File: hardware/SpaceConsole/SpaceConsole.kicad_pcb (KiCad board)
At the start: 2 copper layers, 10 parts, among them IC1 ArduinoProMini, J1 Screw_Terminal_01x03, J2 Screw_Terminal_01x03, J3 Screw_Terminal_01x03, J4 Screw_Terminal_01x03, J5 Screw_Terminal_01x03, J6 Screw_Terminal_01x02, J7 Screw_Terminal_01x02, J8 Conn_01x09_Male, U1 LM2596_Adj_Stepdown_Module

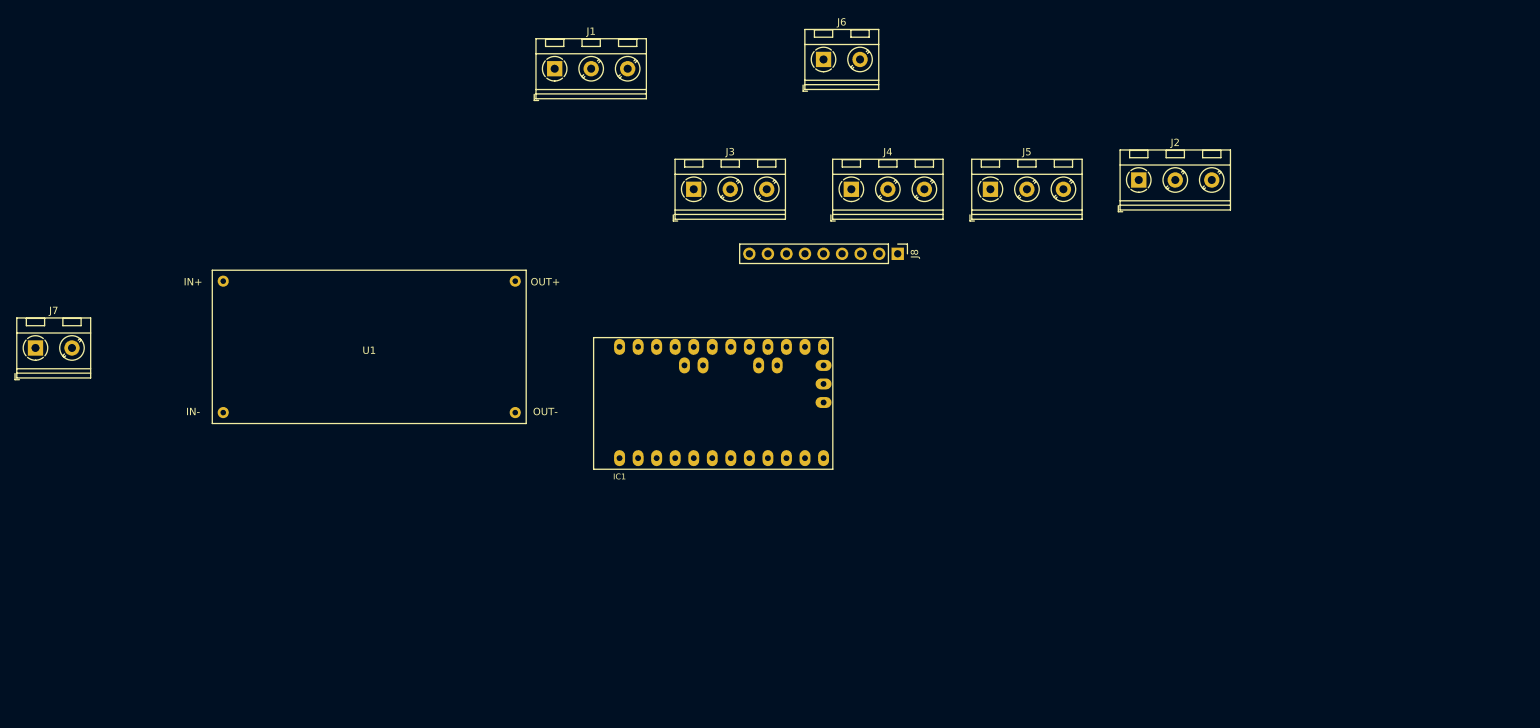
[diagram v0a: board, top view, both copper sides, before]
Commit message: PCB layed out (no traces yet)
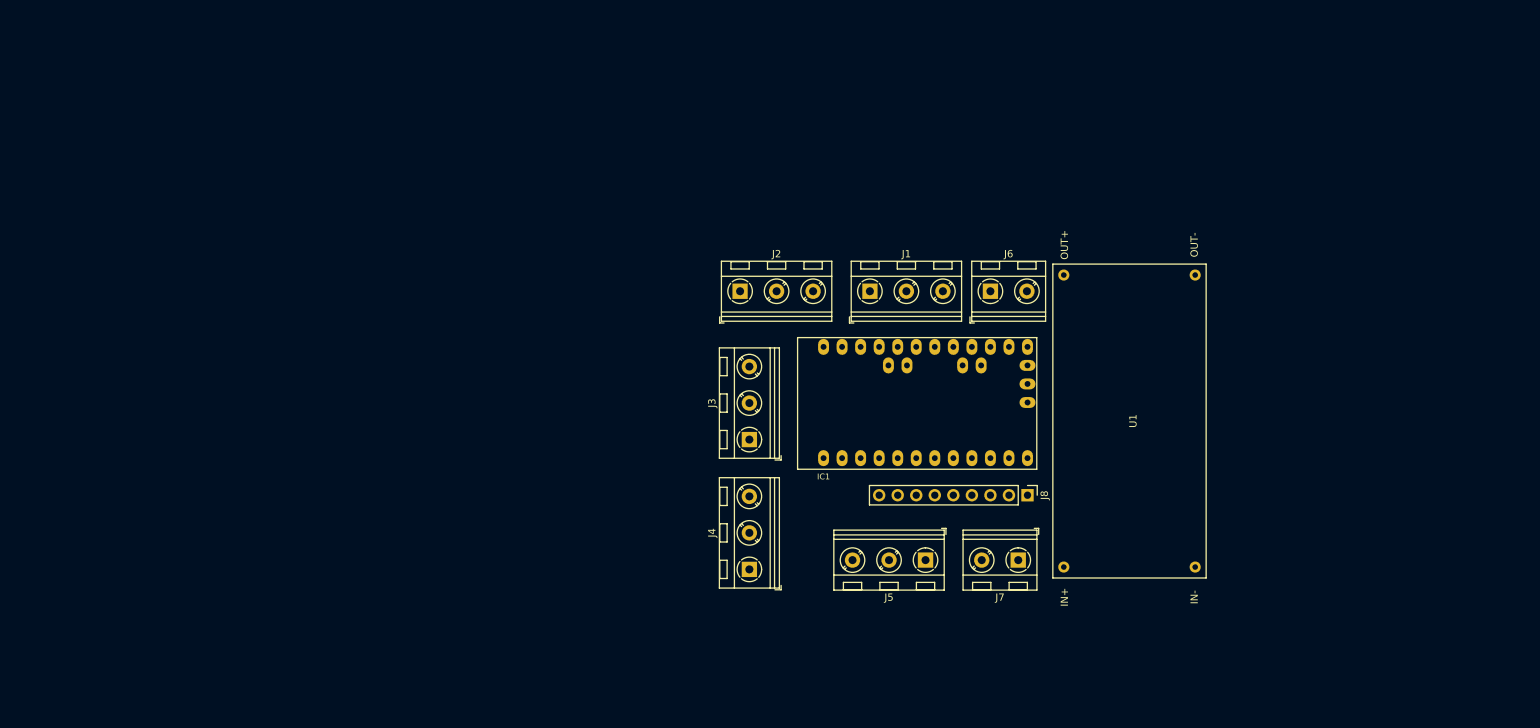
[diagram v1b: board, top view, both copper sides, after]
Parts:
- J1: value Screw_Terminal_01x03 -> LeftFrontLED
- J2: value Screw_Terminal_01x03 -> RightFrontLED
- J3: value Screw_Terminal_01x03 -> LeftMiddleLED
- J4: value Screw_Terminal_01x03 -> RightMiddleLED
- J5: value Screw_Terminal_01x03 -> RearLED
- J6: value Screw_Terminal_01x02 -> SwitchA
- J7: value Screw_Terminal_01x02 -> BatteryIN
- moved J7 137.7 mm to (176.5, 120.7), turned to 180 degrees
- moved U1 104.6 mm to (191.8, 101.6), turned to 90 degrees
- moved J2 56.7 mm to (138.4, 83.8)
- moved J4 53.9 mm to (139.7, 121.9), turned to 90 degrees
- moved J1 52.9 mm to (156.2, 83.8)
- moved J5 51.6 mm to (163.8, 120.7), turned to 180 degrees
- moved J6 39.1 mm to (172.7, 83.8)
- moved J8 37.5 mm to (177.8, 111.8)
- moved J3 35.1 mm to (139.7, 104.1), turned to 90 degrees
- moved IC1 27.9 mm to (163.8, 99.1)

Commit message: Routing done
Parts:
- moved J8 36.8 mm to (141.0, 111.8), turned to 90 degrees
- moved J6 33.0 mm to (139.7, 83.8)
- moved J2 12.7 mm to (151.1, 83.8)
- moved J1 11.4 mm to (167.6, 83.8)
- moved J4 6.48 mm to (146.1, 120.7), turned to 180 degrees
- turned IC1 to 180 degrees
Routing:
- net VCC: track 0.00 -> 109.3 mm
- net /RightMiddleLED: track 0.00 -> 52.8 mm
- net /RearLED: track 0.00 -> 30.7 mm
- net /Battery-: track 0.00 -> 30.5 mm
- net /LeftMiddleLED: track 0.00 -> 27.9 mm
- net /SwitchB: track 0.00 -> 26.7 mm
- net /SwitchC: track 0.00 -> 21.0 mm
- net /SwitchA: track 0.00 -> 18.4 mm
- net /RightFrontLED: track 0.00 -> 12.1 mm
- net /LeftFrontLED: track 0.00 -> 9.69 mm
- net /Battery+: track 0.00 -> 6.63 mm
- net /KnobB1: track 0.00 -> 5.61 mm
- net /KnobB0: track 0.00 -> 5.61 mm
- net /KnobA1: track 0.00 -> 5.61 mm
- net /KnobA0: track 0.00 -> 5.61 mm
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- added copper zone on B.Cu, net GND

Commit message: Remove extra pins from pro
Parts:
- J7: value BatteryIN -> Battery
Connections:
- IC1 pad 21: VCC -> Net-(IC1-Pad21)
- IC1 pad 23: Net-(IC1-Pad23) -> GND
- IC1 pad 24: GND -> VCC
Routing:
- net VCC: track 109.3 -> 129.0 mm

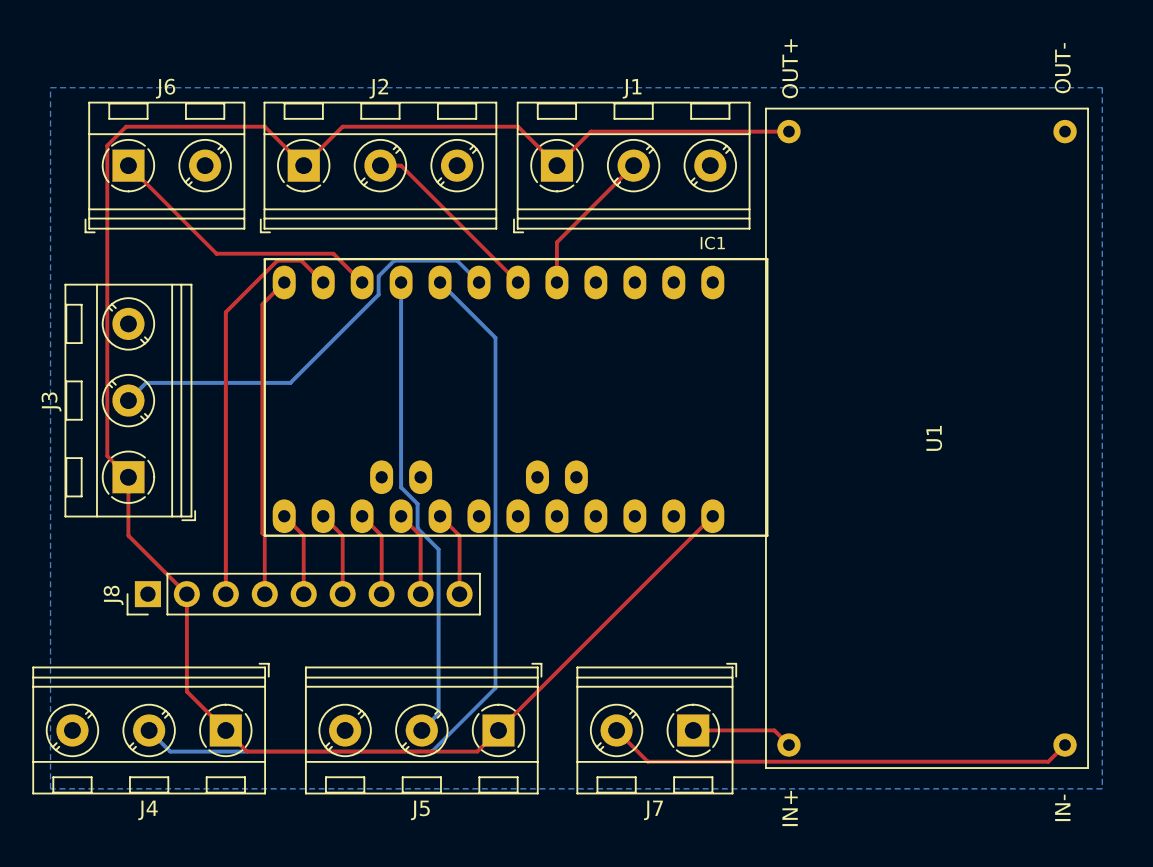
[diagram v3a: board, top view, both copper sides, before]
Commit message: Thicker power traces, add edge cutout
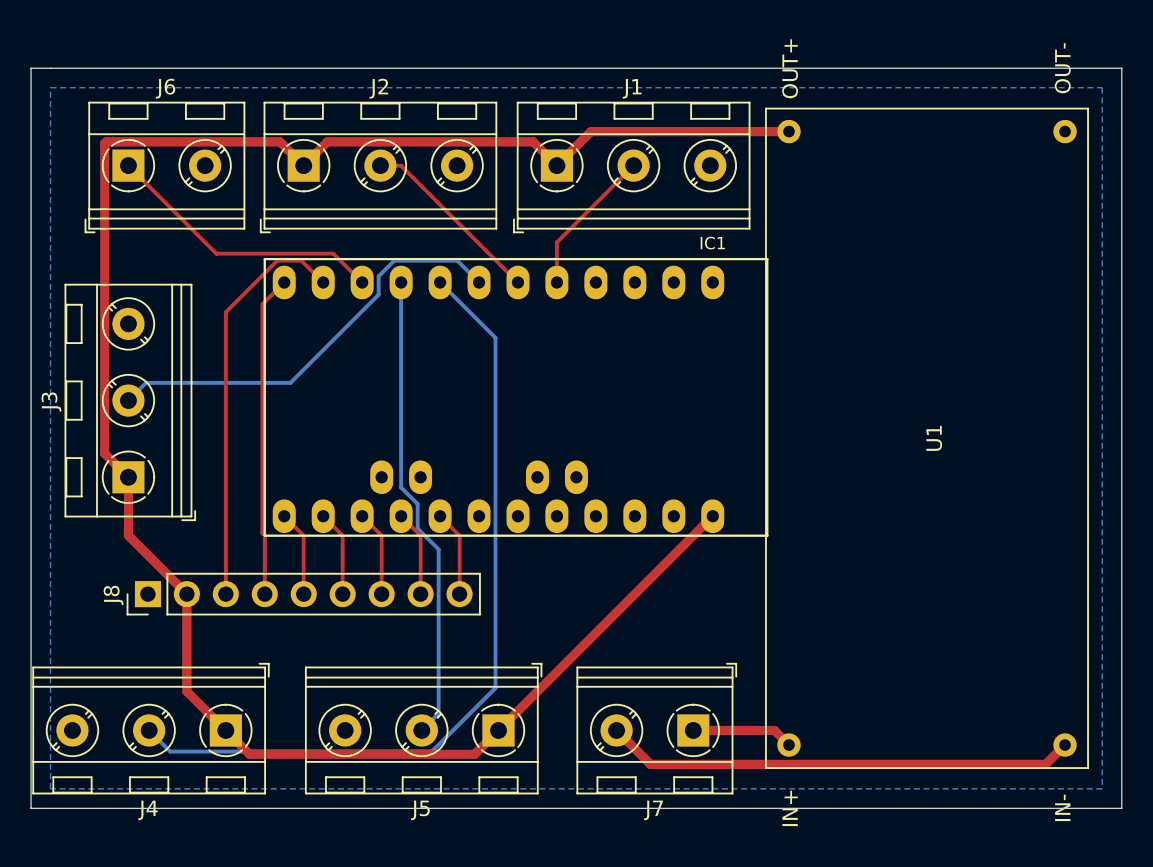
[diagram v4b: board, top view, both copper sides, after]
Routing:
- net VCC: track 129.0 -> 127.9 mm
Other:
- board outline added: 71.1 x 48.3 mm
- net class Power added: clearance 0.2, trace_width 0.6, via_dia 0.8, via_drill 0.4
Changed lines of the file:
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@@
   (general
     (thickness 1.6)
-    (drawings 0)
+    (drawings 5)
     (tracks 66)
     (zones 0)
@@
     (uvia_dia 0.3)
     (uvia_drill 0.1)
-    (add_net /Battery+)
-    (add_net /Battery-)
     (add_net /HornOut)
     (add_net /KnobA0)
@@
     (add_net "Net-(IC1-Pad3)")
     (add_net "Net-(IC1-Pad4)")
+  )
+  (net_class Power ""
+    (clearance 0.2)
+    (trace_width 0.6)
+    (via_dia 0.8)
+    (via_drill 0.4)
+    (uvia_dia 0.3)
+    (uvia_drill 0.1)
+    (add_net /Battery+)
+    (add_net /Battery-)
     (add_net VCC)
   )
@@
     )
   )
-  (segment (start 169.86 81.6) (end 167.64 83.82) (width 0.25) (layer F.Cu) (net 7))
-  (segment (start 182.77 81.6) (end 169.86 81.6) (width 0.25) (layer F.Cu) (net 7))
-  (segment (start 167.64 83.82) (end 165.1 81.28) (width 0.25) (layer F.Cu) (net 7))
-  (segment (start 153.67 81.28) (end 151.13 83.82) (width 0.25) (layer F.Cu) (net 7))
-  (segment (start 165.1 81.28) (end 153.67 81.28) (width 0.25) (layer F.Cu) (net 7))
-  (segment (start 151.13 83.82) (end 148.59 81.28) (width 0.25) (layer F.Cu) (net 7))
-  (segment (start 138.324999 102.764999) (end 139.7 104.14) (width 0.25) (layer F.Cu) (net 7))
-  (segment (start 139.554998 81.28) (end 138.324999 82.509999) (width 0.25) (layer F.Cu) (net 7))
-  (segment (start 138.324999 82.509999) (end 138.324999 102.764999) (width 0.25) (layer F.Cu) (net 7))
-  (segment (start 148.59 81.28) (end 139.554998 81.28) (width 0.25) (layer F.Cu) (net 7))
-  (segment (start 139.7 107.95) (end 143.51 111.76) (width 0.25) (layer F.Cu) (net 7))
-  (segment (start 139.7 104.14) (end 139.7 107.95) (width 0.25) (layer F.Cu) (net 7))
-  (segment (start 143.51 118.11) (end 146.05 120.65) (width 0.25) (layer F.Cu) (net 7))
-  (segment (start 143.51 111.76) (end 143.51 118.11) (width 0.25) (layer F.Cu) (net 7))
-  (segment (start 162.454999 122.025001) (end 163.83 120.65) (width 0.25) (layer F.Cu) (net 7))
-  (segment (start 147.425001 122.025001) (end 162.454999 122.025001) (width 0.25) (layer F.Cu) (net 7))
-  (segment (start 146.05 120.65) (end 147.425001 122.025001) (width 0.25) (layer F.Cu) (net 7))
-  (segment (start 163.83 120.65) (end 177.8 106.68) (width 0.25) (layer F.Cu) (net 7))
+  (gr_line (start 133.35 77.47) (end 134.62 77.47) (layer Edge.Cuts) (width 0.05))
+  (gr_line (start 133.35 125.73) (end 133.35 77.47) (layer Edge.Cuts) (width 0.05))
+  (gr_line (start 204.47 125.73) (end 133.35 125.73) (layer Edge.Cuts) (width 0.05))
+  (gr_line (start 204.47 77.47) (end 204.47 125.73) (layer Edge.Cuts) (width 0.05))
+  (gr_line (start 134.62 77.47) (end 204.47 77.47) (layer Edge.Cuts) (width 0.05))
+  (segment (start 169.86 81.6) (end 167.64 83.82) (width 0.6) (layer F.Cu) (net 7))
+  (segment (start 182.77 81.6) (end 169.86 81.6) (width 0.6) (layer F.Cu) (net 7))
+  (segment (start 152.680001 82.269999) (end 151.13 83.82) (width 0.6) (layer F.Cu) (net 7))
+  (segment (start 166.089999 82.269999) (end 152.680001 82.269999) (width 0.6) (layer F.Cu) (net 7))
+  (segment (start 167.64 83.82) (end 166.089999 82.269999) (width 0.6) (layer F.Cu) (net 7))
+  (segment (start 138.149999 82.369999) (end 138.149999 102.589999) (width 0.6) (layer F.Cu) (net 7))
+  (segment (start 138.149999 102.589999) (end 139.7 104.14) (width 0.6) (layer F.Cu) (net 7))
+  (segment (start 138.249999 82.269999) (end 138.149999 82.369999) (width 0.6) (layer F.Cu) (net 7))
+  (segment (start 149.579999 82.269999) (end 138.249999 82.269999) (width 0.6) (layer F.Cu) (net 7))
+  (segment (start 151.13 83.82) (end 149.579999 82.269999) (width 0.6) (layer F.Cu) (net 7))
+  (segment (start 139.7 107.95) (end 143.51 111.76) (width 0.6) (layer F.Cu) (net 7))
+  (segment (start 139.7 104.14) (end 139.7 107.95) (width 0.6) (layer F.Cu) (net 7))
+  (segment (start 143.51 118.11) (end 146.05 120.65) (width 0.6) (layer F.Cu) (net 7))
+  (segment (start 143.51 111.76) (end 143.51 118.11) (width 0.6) (layer F.Cu) (net 7))
+  (segment (start 162.279999 122.200001) (end 163.83 120.65) (width 0.6) (layer F.Cu) (net 7))
+  (segment (start 147.600001 122.200001) (end 162.279999 122.200001) (width 0.6) (layer F.Cu) (net 7))
+  (segment (start 146.05 120.65) (end 147.600001 122.200001) (width 0.6) (layer F.Cu) (net 7))
+  (segment (start 163.83 120.65) (end 177.8 106.68) (width 0.6) (layer F.Cu) (net 7))
   (segment (start 161.29 107.95) (end 160.02 106.68) (width 0.25) (layer F.Cu) (net 11))
   (segment (start 161.29 111.76) (end 161.29 107.95) (width 0.25) (layer F.Cu) (net 11))
@@
   (segment (start 167.64 88.82) (end 172.64 83.82) (width 0.25) (layer F.Cu) (net 23))
   (segment (start 167.64 91.44) (end 167.64 88.82) (width 0.25) (layer F.Cu) (net 23))
-  (segment (start 199.682999 122.687001) (end 200.77 121.6) (width 0.25) (layer F.Cu) (net 28))
-  (segment (start 173.567001 122.687001) (end 199.682999 122.687001) (width 0.25) (layer F.Cu) (net 28))
-  (segment (start 171.53 120.65) (end 173.567001 122.687001) (width 0.25) (layer F.Cu) (net 28))
-  (segment (start 181.82 120.65) (end 182.77 121.6) (width 0.25) (layer F.Cu) (net 29))
-  (segment (start 176.53 120.65) (end 181.82 120.65) (width 0.25) (layer F.Cu) (net 29))
+  (segment (start 199.507999 122.862001) (end 200.77 121.6) (width 0.6) (layer F.Cu) (net 28))
+  (segment (start 173.742001 122.862001) (end 199.507999 122.862001) (width 0.6) (layer F.Cu) (net 28))
+  (segment (start 171.53 120.65) (end 173.742001 122.862001) (width 0.6) (layer F.Cu) (net 28))
+  (segment (start 181.82 120.65) (end 182.77 121.6) (width 0.6) (layer F.Cu) (net 29))
+  (segment (start 176.53 120.65) (end 181.82 120.65) (width 0.6) (layer F.Cu) (net 29))
   (zone (net 5) (net_name GND) (layer B.Cu) (hatch edge 0.508)
     (connect_pads (clearance 0.508))

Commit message: Add power switch
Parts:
- added J9: Power_Switch, Connector_PinHeader_2.54mm:PinHeader_1x02_P2.54mm_Vertical, F.Cu at (170.2, 111.8)
- added REF**: MountingHole_3.2mm_M3, MountingHole:MountingHole_3.2mm_M3, F.Cu at (205.7, 125.7)
- added REF**: MountingHole_3.2mm_M3, MountingHole:MountingHole_3.2mm_M3, F.Cu at (205.7, 77.5)
- added REF**: MountingHole_3.2mm_M3, MountingHole:MountingHole_3.2mm_M3, F.Cu at (133.3, 77.5)
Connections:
- J7 pad 1: /Battery+ -> Net-(J7-Pad1)
- U1 pad 1: /Battery+ -> Net-(J9-Pad2)
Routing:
- net Net-(J9-Pad2): track 0.00 -> 14.1 mm
- net Net-(J7-Pad1): track 0.00 -> 11.5 mm
- net /Battery+: track 6.63 -> 0.00 mm
- net VCC: track 127.9 -> 130.9 mm
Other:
- board size 71.1 x 48.3 mm -> 80 x 55.9 mm

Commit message: Add knobs and switches to schematic
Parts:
- added BZ1: Horn, Buzzer_Beeper:Buzzer_TDK_PS1240P02BT_D12.2mm_H6.5mm, F.Cu at (232.4, 134.6)
- added SW1: KnobB, Connector_PinHeader_2.54mm:PinHeader_1x05_P2.54mm_Vertical, F.Cu at (220.8, 130.1)
- added SW2: KnobA, Connector_PinHeader_2.54mm:PinHeader_1x05_P2.54mm_Vertical, F.Cu at (225.5, 130.1)
- added SW3: SwitchB, Connector_PinHeader_2.54mm:PinHeader_1x02_P2.54mm_Vertical, F.Cu at (244.1, 130.1)
- added SW4: SwitchC, Connector_PinHeader_2.54mm:PinHeader_1x02_P2.54mm_Vertical, F.Cu at (244.1, 137.3)
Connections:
- net Net-(IC1-Pad18) renamed /SwitchD
- net Net-(IC1-Pad19) renamed /SwitchE
- U1 pad 1: Net-(J9-Pad2) -> Net-(U1-Pad1)
